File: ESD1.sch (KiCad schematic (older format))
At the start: 2 parts, among them U8 USBLC6-2SC6

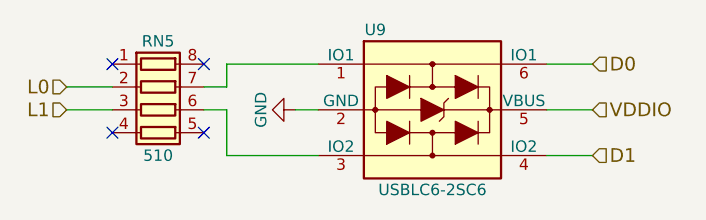
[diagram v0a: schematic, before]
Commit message: Changing the power delivery subsystem.
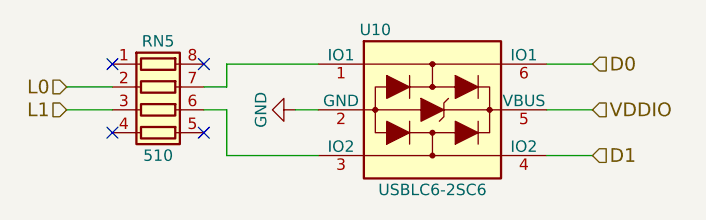
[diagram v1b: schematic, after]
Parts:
- renumbered U8 to U9
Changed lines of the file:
@@
 LIBS:zetex
 LIBS:Zilog
+LIBS:DAP42-cache
 EELAYER 25 0
 EELAYER END
@@
 $EndDescr
 $Comp
-L USBLC6-2SC6 U8
+L USBLC6-2SC6 U9
 U 1 1 59FB205F
 P 6000 3600
-AR Path="/59FB1FB1/59FB205F" Ref="U8"  Part="1"
-AR Path="/59FB2F1A/59FB205F" Ref="U9"  Part="1"
-F 0 "U9" H 5750 3950 50  0000 C CNN
+AR Path="/59FB1FB1/59FB205F" Ref="U9"  Part="1"
+AR Path="/59FB2F1A/59FB205F" Ref="U10"  Part="1"
+F 0 "U10" H 5750 3950 50  0000 C CNN
 F 1 "USBLC6-2SC6" H 6000 3250 50  0000 C CNN
 F 2 "TO_SOT_Packages_SMD:SOT-23-6_Handsoldering" H 6650 3950 50  0001 C CNN
@@
 $EndComp
 $Comp
-L GND #PWR029
+L GND #PWR030
 U 1 1 59FB20BD
 P 5400 3600
-AR Path="/59FB1FB1/59FB20BD" Ref="#PWR029"  Part="1"
-AR Path="/59FB2F1A/59FB20BD" Ref="#PWR030"  Part="1"
-F 0 "#PWR030" H 5400 3350 50  0001 C CNN
+AR Path="/59FB1FB1/59FB20BD" Ref="#PWR030"  Part="1"
+AR Path="/59FB2F1A/59FB20BD" Ref="#PWR031"  Part="1"
+F 0 "#PWR031" H 5400 3350 50  0001 C CNN
 F 1 "GND" H 5400 3450 50  0000 C CNN
 F 2 "" H 5400 3600 50  0001 C CNN
